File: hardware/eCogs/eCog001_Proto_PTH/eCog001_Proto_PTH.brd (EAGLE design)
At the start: 47.5 x 28 mm, 24 parts, among them P1 M10NO_SILK, P2 M10NO_SILK, P3 M10NO_SILK, P4 M10NO_SILK, P5 M10NO_SILK, P6 M10NO_SILK, P7 M10NO_SILK, P8 M10NO_SILK

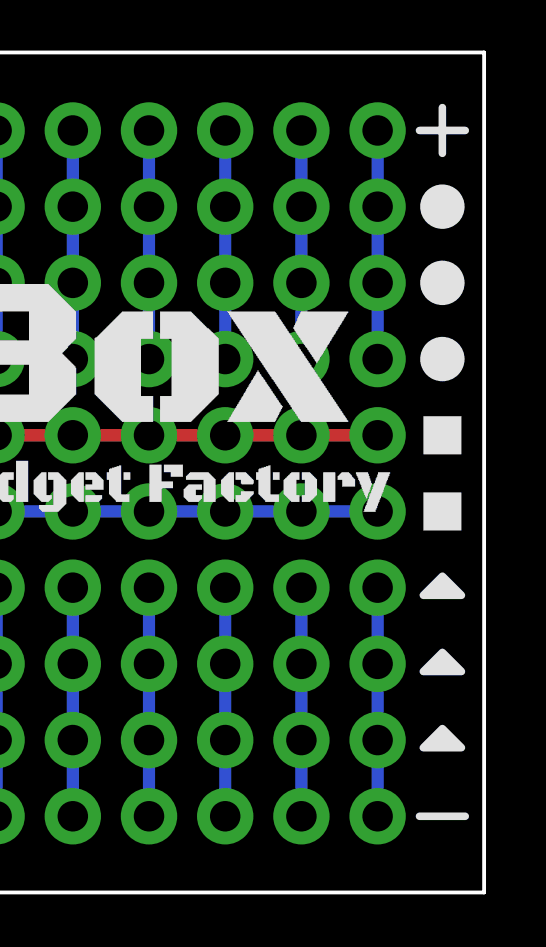
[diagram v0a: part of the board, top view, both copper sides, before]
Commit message: silk adjustments
moved bottom silk labels to edge
replaced pin usage symols with sharpie area
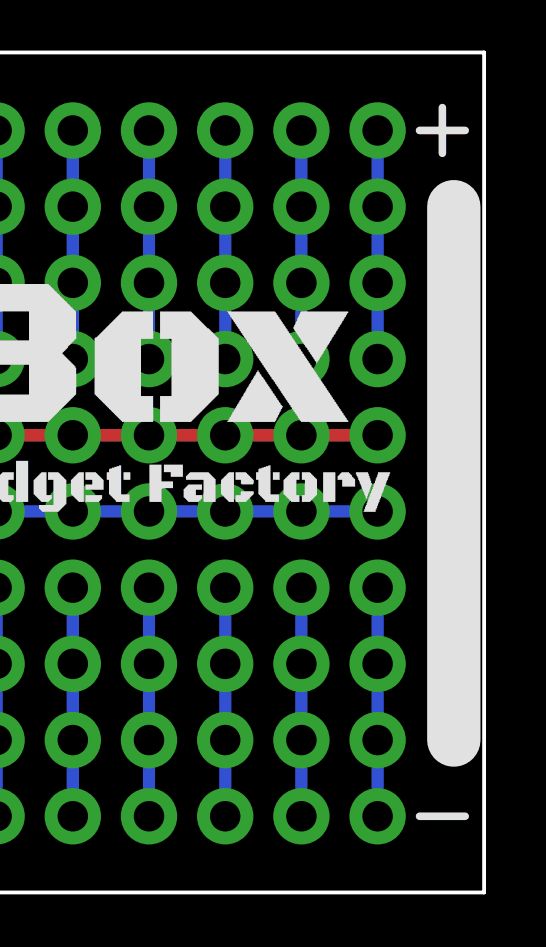
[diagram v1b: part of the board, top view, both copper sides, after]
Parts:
- removed U$2, U$3, U$4: (no value), eCogs:LEGEND_DIO
- removed U$5, U$6: (no value), eCogs:LEGEND_PWM
- removed U$7, U$8, U$9: (no value), eCogs:LEGEND_ANALOG
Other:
- board text added: "ecog001.GadgetFactory.net"
- board text removed: "ecog100.GadgetFactory.net"
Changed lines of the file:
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@@
 <board>
 <plain>
-<text x="37.559" y="18.415" size="0.8128" layer="22" font="vector" rot="MR0">ecog100.GadgetFactory.net</text>
+<text x="43.18" y="26.67" size="0.8128" layer="22" font="vector" rot="MR0">ecog001.GadgetFactory.net</text>
 <text x="46.609" y="16.178" size="1.016" layer="22" font="vector" rot="MR90">ecog001 v1.0</text>
 <text x="46.609" y="6.018" size="1.016" layer="22" font="vector" rot="MR90">Proto PTH</text>
 <text x="46.609" y="0.938" size="1.016" layer="22" font="vector" rot="MR90">eCogs</text>
-<text x="33.782" y="17.526" size="0.6096" layer="22" font="vector" rot="MR0">Copyright 2016</text>
-<text x="35.512" y="16.637" size="0.6096" layer="22" font="vector" rot="MR0">Gadget Factory, LLC</text>
+<text x="43.18" y="1.27" size="0.6096" layer="22" font="vector" rot="MR0" align="top-left">Copyright 2016</text>
+<text x="33.02" y="1.27" size="0.6096" layer="22" font="vector" rot="MR0" align="top-left">Gadget Factory, LLC</text>
 <wire x1="45.847" y1="25.4" x2="47.371" y2="25.4" width="0.254" layer="21"/>
 <wire x1="46.609" y1="26.162" x2="46.609" y2="24.638" width="0.254" layer="21"/>
@@
 <text x="20.32" y="12.7" size="1.016" layer="22" font="vector" rot="MR0" align="center-left">GND</text>
 <text x="20.32" y="15.24" size="1.016" layer="22" font="vector" rot="MR0" align="center-left">3.3V</text>
+<wire x1="46.99" y1="22.86" x2="46.99" y2="5.08" width="1.778" layer="21"/>
 </plain>
 <attributes>
@@
 </autorouter>
 <elements>
-<element name="U$2" library="eCogs" package="LEGEND_DIO" value="" x="46.609" y="22.86"/>
-<element name="U$3" library="eCogs" package="LEGEND_DIO" value="" x="46.609" y="20.32"/>
-<element name="U$5" library="eCogs" package="LEGEND_PWM" value="" x="46.609" y="15.24"/>
-<element name="U$6" library="eCogs" package="LEGEND_PWM" value="" x="46.609" y="12.7"/>
-<element name="U$7" library="eCogs" package="LEGEND_ANALOG" value="" x="46.609" y="10.16"/>
-<element name="U$8" library="eCogs" package="LEGEND_ANALOG" value="" x="46.609" y="7.62"/>
-<element name="U$9" library="eCogs" package="LEGEND_ANALOG" value="" x="46.609" y="5.08"/>
 <element name="U$1" library="GadgetFactory" package="GADGETBOX_TEXT" value="" x="22.352" y="17.399"/>
 <element name="U$10" library="ohw-logo" package="OSHW_FILLX350_NOTEXT" value="" x="11.43" y="2.54"/>
-<element name="U$4" library="eCogs" package="LEGEND_DIO" value="" x="46.609" y="17.78"/>
 <element name="ECOG" library="eCogs" package="ECOG_DUAL_TH" value="ECOG_DUALTHROUGHHOLE" x="0" y="0"/>
 <element name="VCC" library="SparkFun-Connectors" package="1X10_NO_SILK" value="M10NO_SILK" x="21.59" y="15.24" smashed="yes">
